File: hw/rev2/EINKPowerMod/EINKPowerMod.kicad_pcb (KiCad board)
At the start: 2 copper layers, 26 x 30 mm, 67 parts, among them J1 Conn_01x01, J10 Conn_01x01, J11 Conn_01x01, J12 Conn_01x01, J13 Conn_01x01, J14 Conn_01x01, J2 Conn_01x01, J3 Conn_01x01, J4 Conn_01x01, J5 Conn_01x01, J6 Conn_01x01, J7 Conn_01x01, J8 Conn_01x01, J9 Conn_01x01, U1 LM358, U2 LT1945, U3 LT1945, U4 XC6220B331MR-G

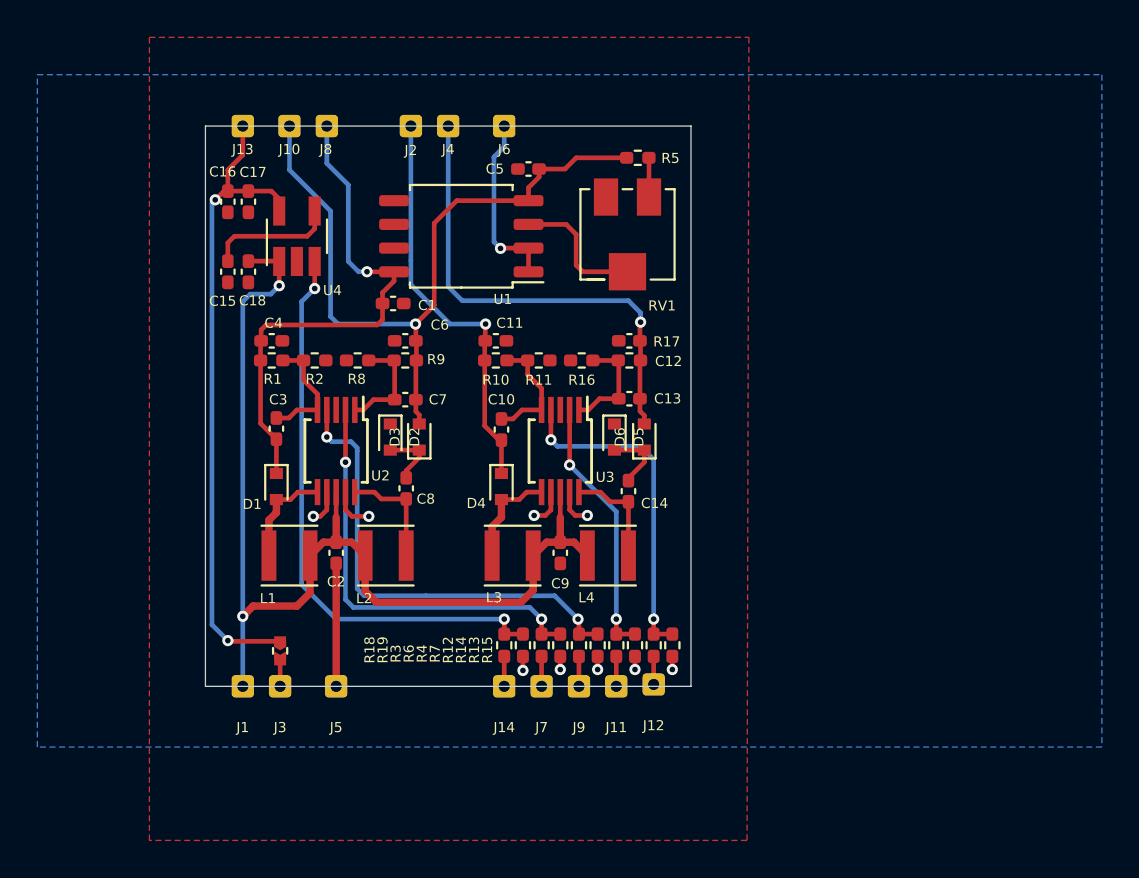
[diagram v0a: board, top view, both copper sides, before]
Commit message: fixed incorrect connection
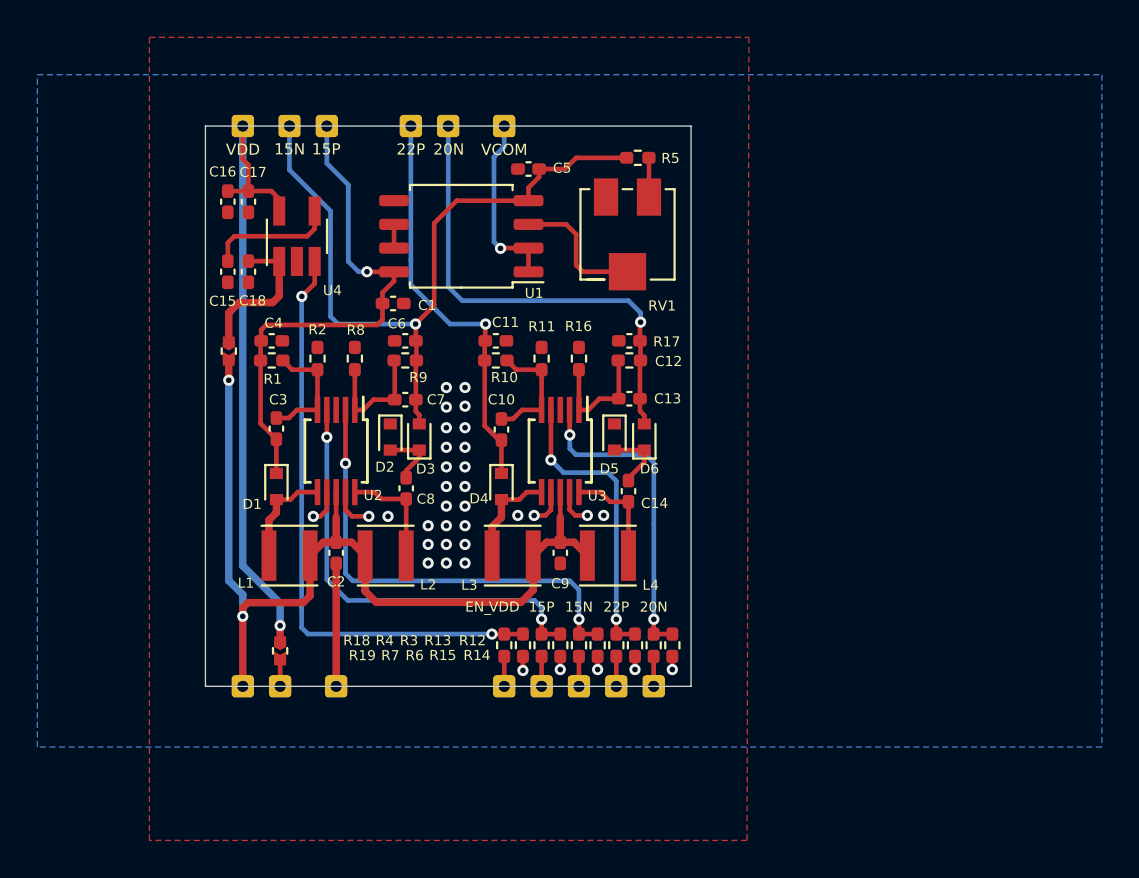
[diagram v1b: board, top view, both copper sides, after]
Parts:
- added JP2: Close, FlightComputer_Library:Jumper_0402_1005Metric, F.Cu at (113.2, 93.8)
- JP1: value SolderJumper_2_Open -> Open
- R1: value 2M -> 300K
- R2: value 120K -> 27K
- R8: value 39K -> 10K
- R9: value 560K -> 110K
- moved R13 2.00 mm to (134.0, 109.5)
- moved R12 2.00 mm to (136.0, 109.5)
- moved R14 2.00 mm to (137.0, 109.5)
- moved R15 2.00 mm to (135.0, 109.5)
- moved R3 2.00 mm to (132.0, 109.5)
- moved R4 2.00 mm to (130.0, 109.5)
- moved R6 2.00 mm to (133.0, 109.5)
- moved R7 2.00 mm to (131.0, 109.5)
- moved R11 0.18 mm to (130.0, 94.2), turned to 90 degrees
- moved R16 0.18 mm to (132.0, 94.2), turned to 90 degrees
- moved R2 0.18 mm to (118.0, 94.2), turned to 90 degrees
- moved R8 0.18 mm to (120.0, 94.2), turned to 90 degrees
- moved J12 0.10 mm to (136.0, 111.8)
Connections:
- C18 pad 2: VCC_5V -> Net-(C18-Pad2)
- R12 pad 2: /EN_22P -> /EN_20N
- R13 pad 2: /EN_20N -> /EN_22P
- R3 pad 2: /EN_15P -> /EN_15N
- R4 pad 2: /EN_15N -> /EN_15P
- U1 pad 5: (no net) -> GND
- U1 pad 6: (no net) -> Net-(U1-Pad6)
- U1 pad 7: (no net) -> Net-(U1-Pad6)
- U4 pad 1: VCC_5V -> Net-(C18-Pad2)
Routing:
- net Net-(C18-Pad2): track 0.00 -> 8.12 mm
- net VCC_5V: track 57.3 -> 49.5 mm
- net Net-(R12-Pad1): track 14.0 -> 17.1 mm
- net Net-(R3-Pad1): track 22.9 -> 25.0 mm
- net Net-(R13-Pad1): track 17.9 -> 15.8 mm
- net Net-(R4-Pad1): track 25.2 -> 23.6 mm
- net Net-(U1-Pad6): track 0.00 -> 1.27 mm
- net Net-(R18-Pad2): track 31.0 -> 31.9 mm
- net Net-(C13-Pad1): track 5.80 -> 6.60 mm
- net Net-(C7-Pad1): track 5.83 -> 6.63 mm
- net VCC_EINK: track 34.7 -> 35.0 mm, vias 2 -> 1
- net GND: vias 9 -> 35
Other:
- board text added: "15N"
- board text added: "15P"
- board text added: "20N"
- board text added: "22P"
- board text added: "EN_"
- board text added: "VCOM"
- board text added: "VDD"

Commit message: re-numbering
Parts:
- removed R13, R18: 33R, FlightComputer_Library:R_0402_1005Metric_Pad0.72x0.64mm_HandSolder
- removed R14, R7: 100K, FlightComputer_Library:R_0402_1005Metric_Pad0.72x0.64mm_HandSolder
- removed R17: 560K, FlightComputer_Library:R_0402_1005Metric_Pad0.72x0.64mm_HandSolder
- added R1002: 33R, FlightComputer_Library:R_0402_1005Metric_Pad0.72x0.64mm_HandSolder, F.Cu at (134.0, 109.5)
- added R1005: 100K, FlightComputer_Library:R_0402_1005Metric_Pad0.72x0.64mm_HandSolder, F.Cu at (137.0, 109.5)
- added R1007: 33R, FlightComputer_Library:R_0402_1005Metric_Pad0.72x0.64mm_HandSolder, F.Cu at (128.0, 109.5)
- added R1010: 100K, FlightComputer_Library:R_0402_1005Metric_Pad0.72x0.64mm_HandSolder, F.Cu at (131.0, 109.5)
- added R1016: 560K, FlightComputer_Library:R_0402_1005Metric_Pad0.72x0.64mm_HandSolder, F.Cu at (134.7, 94.3)
- turned R1006 to 90 degrees
- turned R1008 to 90 degrees
- turned R1009 to 90 degrees
- renumbered C9 to C1001, C2 to C1002, C18 to C1003, C15 to C1004, C14 to C1005, C8 to C1006, C16 to C1007, C10 to C1008, C3 to C1009, C17 to C1010, C13 to C1011, C7 to C1012, C11 to C1013, C4 to C1014, C12 to C1015, C6 to C1016, C1 to C1017, C5 to C1018, D4 to D1001, D1 to D1002, D5 to D1003, D2 to D1004, D6 to D1005, D3 to D1006, J1 to J1001, J3 to J1002, J5 to J1003, J7 to J1004, J9 to J1005, J11 to J1006, J12 to J1007, J14 to J1008, J2 to J1009, J4 to J1010, J6 to J1011, J8 to J1012, J10 to J1013, J13 to J1014, JP2 to JP1001, JP1 to JP1002, L3 to L1001, L1 to L1002, L4 to L1003, L2 to L1004, R12 to R1001, R3 to R1003, R4 to R1004, R6 to R1006, R15 to R1008, R19 to R1009, R10 to R1011, R11 to R1012, R1 to R1013, R2 to R1014, R16 to R1015, R8 to R1017, R9 to R1018, R5 to R1019, RV1 to RV1001, U4 to U1001, U3 to U1002, U2 to U1003, U1 to U1004
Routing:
- net GND: track 17.9 -> 14.3 mm, vias 35 -> 16
- net Net-(R1002-Pad1): track 15.8 -> 16.5 mm
- net Net-(R1004-Pad1): track 23.6 -> 24.2 mm
- net Net-(R1001-Pad1): track 17.1 -> 17.7 mm
- net Net-(R1007-Pad2): track 31.9 -> 32.5 mm
- net Net-(R1003-Pad1): track 25.0 -> 25.6 mm
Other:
- board text added: "3V3"
- board text added: "5V"

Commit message: on/off vcom
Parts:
- added C1019: 0.1uF, FlightComputer_Library:C_0402_1005Metric_Pad0.74x0.62mm_HandSolder, F.Cu at (136.3, 89.0)
- added JP1003: Open, FlightComputer_Library:Jumper_0402_1005Metric, F.Cu at (133.3, 91.2)
- added U1005: NC7SB3157P6X, Package_TO_SOT_SMD:SOT-363_SC-70-6, F.Cu at (133.3, 89.0)
- moved R1019 9.42 mm to (125.8, 84.0)
- moved C1004 6.75 mm to (117.1, 84.1), turned to 0 degrees
- moved C1018 6.61 mm to (122.7, 84.0)
- moved RV1001 3.01 mm to (134.6, 84.5), turned to 180 degrees
- moved C1010 1.79 mm to (114.7, 84.0), turned to 0 degrees
- moved U1004 1.31 mm to (124.4, 87.6)
- moved C1003 1.19 mm to (113.3, 89.0), turned to 270 degrees
- moved U1001 0.72 mm to (116.2, 87.6)
- moved C1017 0.71 mm to (121.3, 91.3)
- moved C1007 0.54 mm to (113.3, 86.3)
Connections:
- net /EN_VCC_EINK renamed /EN_VCOM
- U1001 pad 3: Net-(R1007-Pad2) -> Net-(C1003-Pad2)
- U1004 pad 1: VCOM -> Net-(JP1003-Pad1)
- U1004 pad 2: VCOM -> Net-(JP1003-Pad1)
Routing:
- net VCC_3V3: track 1.04 -> 48.3 mm, vias 0 -> 1
- net Net-(JP1003-Pad1): track 0.00 -> 7.39 mm
- net VCOM: track 9.35 -> 14.5 mm
- net Net-(R1019-Pad1): track 2.10 -> 6.55 mm
- net Net-(C1004-Pad2): track 6.89 -> 2.47 mm
- net -15V: track 39.2 -> 35.4 mm
- net Net-(RV1001-Pad2): track 7.32 -> 10.5 mm
- net Net-(C1003-Pad2): track 8.12 -> 10.3 mm
- net Net-(R1007-Pad2): track 32.5 -> 34.5 mm
- net +15V: track 27.6 -> 26.2 mm
- net VCC_5V: track 49.5 -> 50.7 mm
- net VCC_EINK: track 35.0 -> 34.4 mm
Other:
- board text added: "EPD Power management"
